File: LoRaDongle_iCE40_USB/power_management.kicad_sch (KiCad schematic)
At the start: 17 parts, among them U1 RP550K0001A-TR

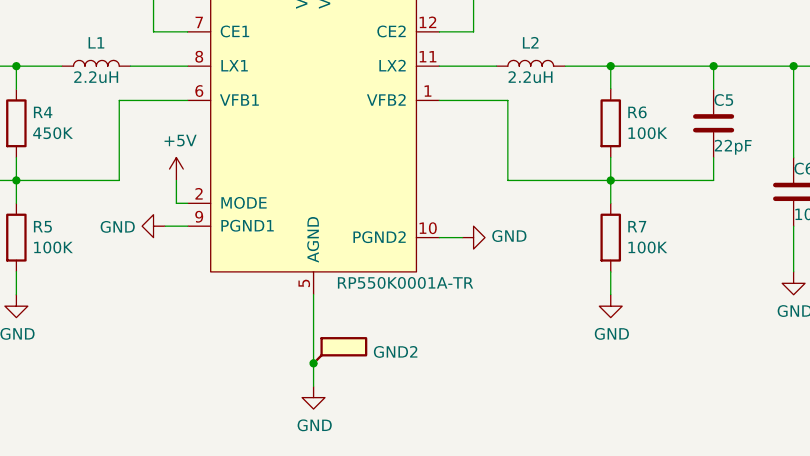
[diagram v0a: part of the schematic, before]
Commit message: updating symbol details
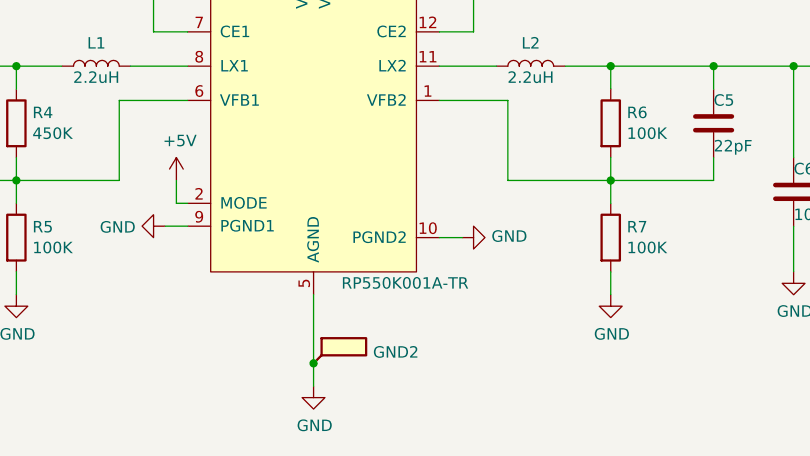
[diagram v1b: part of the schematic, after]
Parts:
- 1V2, 3V3, GND2: Manufacturer (none) -> -; Manufacturer Part Number (none) -> -; Package (none) -> -; Type (none) -> -
- C2, C4, C6: Manufacturer Part Number (none) -> Out of Stock find New; Package (none) -> 0603; Type (none) -> SMD
- C3, C5: Manufacturer (none) -> Murata Electronics; Manufacturer Part Number (none) -> GRM1555C1H220FA01D; Package (none) -> 0402; Type (none) -> SMD
- L1, L2: Manufacturer (none) -> Taiyo Yuden; Manufacturer Part Number (none) -> MCHK1608T2R2MKN; Package (none) -> 0603; Physical Size 1008 -> (none); Type (none) -> SMD
- U1: value RP550K0001A-TR -> RP550K001A-TR; Manufacturer (none) -> Nisshinbo Micro Devices Inc.; Manufacturer Part Number (none) -> RP550K001A-TR; Package (none) -> DFN(PLP)2730-12; Type (none) -> SMD
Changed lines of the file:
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@@
     (in_bom yes) (on_board yes)
     (property "Reference" "U1" (id 0) (at 139.7 77.47 0))
-    (property "Value" "RP550K0001A-TR" (id 1) (at 161.29 113.03 0))
+    (property "Value" "RP550K001A-TR" (id 1) (at 161.29 113.03 0))
     (property "Footprint" "RP550K001A-TR_KiCad:SON50P270X300X60-13N" (id 2) (at 137.16 80.01 0)
       (effects (font (size 1.27 1.27)) hide)
     )
     (property "Datasheet" "" (id 3) (at 137.16 80.01 0)
+      (effects (font (size 1.27 1.27)) hide)
+    )
+    (property "Description" "BUCK DC/DC CONVERTER DUAL OUTPUT" (id 4) (at 151.13 96.52 0)
+      (effects (font (size 1.27 1.27)) hide)
+    )
+    (property "Manufacturer" "Nisshinbo Micro Devices Inc." (id 5) (at 151.13 96.52 0)
+      (effects (font (size 1.27 1.27)) hide)
+    )
+    (property "Manufacturer Part Number" "RP550K001A-TR" (id 6) (at 151.13 96.52 0)
+      (effects (font (size 1.27 1.27)) hide)
+    )
+    (property "Package" "DFN(PLP)2730-12" (id 7) (at 151.13 96.52 0)
+      (effects (font (size 1.27 1.27)) hide)
+    )
+    (property "Type" "SMD" (id 8) (at 151.13 96.52 0)
       (effects (font (size 1.27 1.27)) hide)
     )
@@
       (effects (font (size 1.27 1.27)) hide)
     )
+    (property "Description" "CAP CER 22PF 50V C0G/NP0 0402" (id 5) (at 106.68 95.25 0)
+      (effects (font (size 1.27 1.27)) hide)
+    )
+    (property "Manufacturer" "Murata Electronics" (id 6) (at 106.68 95.25 0)
+      (effects (font (size 1.27 1.27)) hide)
+    )
+    (property "Manufacturer Part Number" "GRM1555C1H220FA01D" (id 7) (at 106.68 95.25 0)
+      (effects (font (size 1.27 1.27)) hide)
+    )
+    (property "Package" "0402" (id 8) (at 106.68 95.25 0)
+      (effects (font (size 1.27 1.27)) hide)
+    )
+    (property "Type" "SMD" (id 9) (at 106.68 95.25 0)
+      (effects (font (size 1.27 1.27)) hide)
+    )
     (pin "1")
     (pin "2")
@@
     )
     (property "Physical size" "0603" (id 5) (at 97.79 102.87 0)
+      (effects (font (size 1.27 1.27)) hide)
+    )
+    (property "Manufacturer Part Number" "Out of Stock find New" (id 6) (at 97.79 102.87 0)
+      (effects (font (size 1.27 1.27)) hide)
+    )
+    (property "Package" "0603" (id 7) (at 97.79 102.87 0)
+      (effects (font (size 1.27 1.27)) hide)
+    )
+    (property "Type" "SMD" (id 8) (at 97.79 102.87 0)
       (effects (font (size 1.27 1.27)) hide)
     )
@@
       (effects (font (size 1.27 1.27)) hide)
     )
+    (property "Description" "Test Point" (id 4) (at 93.98 88.9 0)
+      (effects (font (size 1.27 1.27)) hide)
+    )
+    (property "Manufacturer" "-" (id 5) (at 93.98 88.9 0)
+      (effects (font (size 1.27 1.27)) hide)
+    )
+    (property "Manufacturer Part Number" "-" (id 6) (at 93.98 88.9 0)
+      (effects (font (size 1.27 1.27)) hide)
+    )
+    (property "Package" "-" (id 7) (at 93.98 88.9 0)
+      (effects (font (size 1.27 1.27)) hide)
+    )
+    (property "Type" "-" (id 8) (at 93.98 88.9 0)
+      (effects (font (size 1.27 1.27)) hide)
+    )
     (pin "1")
   )
@@
       (effects (font (size 1.27 1.27)) hide)
     )
+    (property "Description" "Test Point" (id 4) (at 209.55 88.9 0)
+      (effects (font (size 1.27 1.27)) hide)
+    )
+    (property "Manufacturer" "-" (id 5) (at 209.55 88.9 0)
+      (effects (font (size 1.27 1.27)) hide)
+    )
+    (property "Manufacturer Part Number" "-" (id 6) (at 209.55 88.9 0)
+      (effects (font (size 1.27 1.27)) hide)
+    )
+    (property "Package" "-" (id 7) (at 209.55 88.9 0)
+      (effects (font (size 1.27 1.27)) hide)
+    )
+    (property "Type" "-" (id 8) (at 209.55 88.9 0)
+      (effects (font (size 1.27 1.27)) hide)
+    )
     (pin "1")
   )
@@
       (effects (font (size 1.27 1.27)) hide)
     )
+    (property "Description" "Test Point" (id 4) (at 151.13 121.92 0)
+      (effects (font (size 1.27 1.27)) hide)
+    )
+    (property "Manufacturer" "-" (id 5) (at 151.13 121.92 0)
+      (effects (font (size 1.27 1.27)) hide)
+    )
+    (property "Manufacturer Part Number" "-" (id 6) (at 151.13 121.92 0)
+      (effects (font (size 1.27 1.27)) hide)
+    )
+    (property "Package" "-" (id 7) (at 151.13 121.92 0)
+      (effects (font (size 1.27 1.27)) hide)
+    )
+    (property "Type" "-" (id 8) (at 151.13 121.92 0)
+      (effects (font (size 1.27 1.27)) hide)
+    )
     (pin "1")
   )
@@
       (effects (font (size 1.27 1.27)) hide)
     )
+    (property "Manufacturer Part Number" "Out of Stock find New" (id 6) (at 204.47 102.87 0)
+      (effects (font (size 1.27 1.27)) hide)
+    )
+    (property "Package" "0603" (id 7) (at 204.47 102.87 0)
+      (effects (font (size 1.27 1.27)) hide)
+    )
+    (property "Type" "SMD" (id 8) (at 204.47 102.87 0)
+      (effects (font (size 1.27 1.27)) hide)
+    )
     (pin "1")
     (pin "2")
@@
       (effects (font (size 1.27 1.27)) hide)
     )
+    (property "Description" "CAP CER 22PF 50V C0G/NP0 0402" (id 5) (at 195.58 95.25 0)
+      (effects (font (size 1.27 1.27)) hide)
+    )
+    (property "Manufacturer" "Murata Electronics" (id 6) (at 195.58 95.25 0)
+      (effects (font (size 1.27 1.27)) hide)
+    )
+    (property "Manufacturer Part Number" "GRM1555C1H220FA01D" (id 7) (at 195.58 95.25 0)
+      (effects (font (size 1.27 1.27)) hide)
+    )
+    (property "Package" "0402" (id 8) (at 195.58 95.25 0)
+      (effects (font (size 1.27 1.27)) hide)
+    )
+    (property "Type" "SMD" (id 9) (at 195.58 95.25 0)
+      (effects (font (size 1.27 1.27)) hide)
+    )
     (pin "1")
     (pin "2")
@@
     )
     (property "Physical size" "0603" (id 5) (at 115.57 69.85 0)
+      (effects (font (size 1.27 1.27)) hide)
+    )
+    (property "Manufacturer Part Number" "Out of Stock find New" (id 6) (at 115.57 69.85 0)
+      (effects (font (size 1.27 1.27)) hide)
+    )
+    (property "Package" "0603" (id 7) (at 115.57 69.85 0)
+      (effects (font (size 1.27 1.27)) hide)
+    )
+    (property "Type" "SMD" (id 8) (at 115.57 69.85 0)
       (effects (font (size 1.27 1.27)) hide)
     )
@@
       (effects (font (size 1.27 1.27)) hide)
     )
-    (property "Physical Size" "1008" (id 5) (at 175.26 88.9 90)
+    (property "Physical Size" "" (id 5) (at 175.26 88.9 90)
+      (effects (font (size 1.27 1.27)) hide)
+    )
+    (property "Description" "FIXED IND 2.2UH 1.2A 292MOHM SMD" (id 6) (at 175.26 88.9 0)
+      (effects (font (size 1.27 1.27)) hide)
+    )
+    (property "Manufacturer" "Taiyo Yuden" (id 7) (at 175.26 88.9 0)
+      (effects (font (size 1.27 1.27)) hide)
+    )
+    (property "Manufacturer Part Number" "MCHK1608T2R2MKN" (id 8) (at 175.26 88.9 0)
+      (effects (font (size 1.27 1.27)) hide)
+    )
+    (property "Package" "0603" (id 9) (at 175.26 88.9 0)
+      (effects (font (size 1.27 1.27)) hide)
+    )
+    (property "Type" "SMD" (id 10) (at 175.26 88.9 0)
       (effects (font (size 1.27 1.27)) hide)
     )
@@
       (effects (font (size 1.27 1.27)) hide)
     )
-    (property "Physical Size" "1008" (id 5) (at 127 88.9 90)
-      (effects (font (size 1.27 1.27)) hide)
-    )
+    (property "Physical Size" "" (id 5) (at 127 88.9 90)
+      (effects (font (size 1.27 1.27)) hide)
+    )
+    (property "Description" "FIXED IND 2.2UH 1.2A 292MOHM SMD" (id 6) (at 127 88.9 0)
+      (effects (font (size 1.27 1.27)) hide)
+    )
+    (property "Manufacturer" "Taiyo Yuden" (id 7) (at 127 88.9 0)
+      (effects (font (size 1.27 1.27)) hide)
+    )
+    (property "Manufacturer Part Number" "MCHK1608T2R2MKN" (id 8) (at 127 88.9 0)
+      (effects (font (size 1.27 1.27)) hide)
+    )
+    (property "Package" "0603" (id 9) (at 127 88.9 0)
+      (effects (font (size 1.27 1.27)) hide)
+    )
+    (property "Type" "SMD" (id 10) (at 127 88.9 0)
+      (effects (font (size 1.27 1.27)) hide)
+    )

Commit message: updated BOM
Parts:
- C2, C4, C6: Manufacturer (none) -> Murata Electronics; Manufacturer Part Number Out of Stock find New -> GRM188R60J106ME47D
- D1: value LED -> PWR; footprint LED_SMD:LED_0603_1608Metric_Pad1.05x0.95mm_HandSolder -> LED_SMD:LED_0805_2012Metric_Pad1.15x1.40mm_HandSolder; Manufacturer (none) -> SunLED; Manufacturer Part Number (none) -> XZM2CRK54WA-8; Package (none) -> 0805
- R3: value R -> 100R; Manufacturer (none) -> Stackpole Electronics Inc; Manufacturer Part Number (none) -> RMCF0402FT100R; Package (none) -> 0402
- R4: value 450K -> 453K; Manufacturer (none) -> Stackpole Electronics Inc; Manufacturer Part Number (none) -> RMCF0402FT453K
- R5, R6, R7: Manufacturer (none) -> Stackpole Electronics Inc; Manufacturer Part Number (none) -> RMCF0402JT100K
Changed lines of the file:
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@@
+      (effects (font (size 1.27 1.27)) hide)
+    )
+    (property "Description" "RES 100K OHM 5% 1/16W 0402" (id 4) (at 184.15 95.25 0)
+      (effects (font (size 1.27 1.27)) hide)
+    )
+    (property "Manufacturer" "Stackpole Electronics Inc" (id 5) (at 184.15 95.25 0)
+      (effects (font (size 1.27 1.27)) hide)
+    )
+    (property "Manufacturer Part Number" "RMCF0402JT100K" (id 6) (at 184.15 95.25 0)
       (effects (font (size 1.27 1.27)) hide)
     )
@@
     )
     (property "Datasheet" "~" (id 3) (at 184.15 107.95 0)
+      (effects (font (size 1.27 1.27)) hide)
+    )
+    (property "Description" "RES 100K OHM 5% 1/16W 0402" (id 4) (at 184.15 107.95 0)
+      (effects (font (size 1.27 1.27)) hide)
+    )
+    (property "Manufacturer" "Stackpole Electronics Inc" (id 5) (at 184.15 107.95 0)
+      (effects (font (size 1.27 1.27)) hide)
+    )
+    (property "Manufacturer Part Number" "RMCF0402JT100K" (id 6) (at 184.15 107.95 0)
       (effects (font (size 1.27 1.27)) hide)
     )
@@
       (effects (font (size 1.27 1.27)) (justify left))
     )
-    (property "Value" "450K" (id 1) (at 119.888 96.393 0)
+    (property "Value" "453K" (id 1) (at 119.888 96.393 0)
       (effects (font (size 1.27 1.27)) (justify left))
     )
@@
       (effects (font (size 1.27 1.27)) hide)
     )
+    (property "Description" "RES 453K OHM 1% 1/16W 0402" (id 4) (at 118.11 95.25 0)
+      (effects (font (size 1.27 1.27)) hide)
+    )
+    (property "Manufacturer" "Stackpole Electronics Inc" (id 5) (at 118.11 95.25 0)
+      (effects (font (size 1.27 1.27)) hide)
+    )
+    (property "Manufacturer Part Number" "RMCF0402FT453K" (id 6) (at 118.11 95.25 0)
+      (effects (font (size 1.27 1.27)) hide)
+    )
     (pin "1")
     (pin "2")
@@
       (effects (font (size 1.27 1.27)) hide)
     )
+    (property "Description" "RES 100K OHM 5% 1/16W 0402" (id 4) (at 118.11 107.95 0)
+      (effects (font (size 1.27 1.27)) hide)
+    )
+    (property "Manufacturer" "Stackpole Electronics Inc" (id 5) (at 118.11 107.95 0)
+      (effects (font (size 1.27 1.27)) hide)
+    )
+    (property "Manufacturer Part Number" "RMCF0402JT100K" (id 6) (at 118.11 107.95 0)
+      (effects (font (size 1.27 1.27)) hide)
+    )
     (pin "1")
     (pin "2")
@@
       (effects (font (size 1.27 1.27)) hide)
     )
-    (property "Manufacturer Part Number" "Out of Stock find New" (id 6) (at 97.79 102.87 0)
+    (property "Manufacturer Part Number" "GRM188R60J106ME47D" (id 6) (at 97.79 102.87 0)
       (effects (font (size 1.27 1.27)) hide)
     )
@@
     )
     (property "Type" "SMD" (id 8) (at 97.79 102.87 0)
+      (effects (font (size 1.27 1.27)) hide)
+    )
+    (property "Description" "CAP CER 10UF 6.3V X5R 0603" (id 9) (at 97.79 102.87 0)
+      (effects (font (size 1.27 1.27)) hide)
+    )
+    (property "Manufacturer" "Murata Electronics" (id 10) (at 97.79 102.87 0)
       (effects (font (size 1.27 1.27)) hide)
     )
@@
       (effects (font (size 1.27 1.27)) (justify left))
     )
-    (property "Value" "R" (id 1) (at 56.388 96.393 0)
+    (property "Value" "100R" (id 1) (at 56.388 96.393 0)
       (effects (font (size 1.27 1.27)) (justify left))
     )
@@
       (effects (font (size 1.27 1.27)) hide)
     )
+    (property "Description" "RES 100 OHM 1% 1/16W 0402" (id 4) (at 54.61 95.25 0)
+      (effects (font (size 1.27 1.27)) hide)
+    )
+    (property "Manufacturer" "Stackpole Electronics Inc" (id 5) (at 54.61 95.25 0)
+      (effects (font (size 1.27 1.27)) hide)
+    )
+    (property "Manufacturer Part Number" "RMCF0402FT100R" (id 6) (at 54.61 95.25 0)
+      (effects (font (size 1.27 1.27)) hide)
+    )
+    (property "Package" "0402" (id 7) (at 54.61 95.25 0)
+      (effects (font (size 1.27 1.27)) hide)
+    )
     (pin "1")
     (pin "2")
@@
       (effects (font (size 1.27 1.27)) (justify right))
     )
-    (property "Value" "LED" (id 1) (at 57.6072 105.4608 90)
-      (effects (font (size 1.27 1.27)) (justify right))
-    )
-    (property "Footprint" "LED_SMD:LED_0603_1608Metric_Pad1.05x0.95mm_HandSolder" (id 2) (at 54.61 104.14 0)
+    (property "Value" "PWR" (id 1) (at 57.6072 105.4608 90)
+      (effects (font (size 1.27 1.27)) (justify right))
+    )
+    (property "Footprint" "LED_SMD:LED_0805_2012Metric_Pad1.15x1.40mm_HandSolder" (id 2) (at 54.61 104.14 0)
       (effects (font (size 1.27 1.27)) hide)
     )
     (property "Datasheet" "~" (id 3) (at 54.61 104.14 0)
+      (effects (font (size 1.27 1.27)) hide)
+    )
+    (property "Description" "LED RED CLEAR CHIP SMD" (id 4) (at 54.61 104.14 0)
+      (effects (font (size 1.27 1.27)) hide)
+    )
+    (property "Manufacturer" "SunLED" (id 5) (at 54.61 104.14 0)
+      (effects (font (size 1.27 1.27)) hide)
+    )
+    (property "Manufacturer Part Number" "XZM2CRK54WA-8" (id 6) (at 54.61 104.14 0)
+      (effects (font (size 1.27 1.27)) hide)
+    )
+    (property "Package" "0805" (id 7) (at 54.61 104.14 0)
       (effects (font (size 1.27 1.27)) hide)
     )
@@
       (effects (font (size 1.27 1.27)) hide)
     )
-    (property "Manufacturer Part Number" "Out of Stock find New" (id 6) (at 204.47 102.87 0)
+    (property "Manufacturer Part Number" "GRM188R60J106ME47D" (id 6) (at 204.47 102.87 0)
       (effects (font (size 1.27 1.27)) hide)
     )
@@
       (effects (font (size 1.27 1.27)) hide)
     )
+    (property "Description" "CAP CER 10UF 6.3V X5R 0603" (id 9) (at 204.47 102.87 0)
+      (effects (font (size 1.27 1.27)) hide)
+    )
+    (property "Manufacturer" "Murata Electronics" (id 10) (at 204.47 102.87 0)
+      (effects (font (size 1.27 1.27)) hide)
+    )
     (pin "1")
     (pin "2")
@@
       (effects (font (size 1.27 1.27)) hide)
     )
-    (property "Manufacturer Part Number" "Out of Stock find New" (id 6) (at 115.57 69.85 0)
+    (property "Manufacturer Part Number" "GRM188R60J106ME47D" (id 6) (at 115.57 69.85 0)
       (effects (font (size 1.27 1.27)) hide)
     )
@@
       (effects (font (size 1.27 1.27)) hide)
     )
+    (property "Description" "CAP CER 10UF 6.3V X5R 0603" (id 9) (at 115.57 69.85 0)
+      (effects (font (size 1.27 1.27)) hide)
+    )
+    (property "Manufacturer" "Murata Electronics" (id 10) (at 115.57 69.85 0)
+      (effects (font (size 1.27 1.27)) hide)
+    )

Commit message: generate raw bom csv from kicad
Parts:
- R4, R5, R6, R7: Package (none) -> 0402
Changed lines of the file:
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@@
+      (effects (font (size 1.27 1.27)) hide)
+    )
+    (property "Package" "0402" (id 7) (at 184.15 95.25 0)
       (effects (font (size 1.27 1.27)) hide)
     )
@@
     )
     (property "Manufacturer Part Number" "RMCF0402JT100K" (id 6) (at 184.15 107.95 0)
+      (effects (font (size 1.27 1.27)) hide)
+    )
+    (property "Package" "0402" (id 7) (at 184.15 107.95 0)
       (effects (font (size 1.27 1.27)) hide)
     )
@@
       (effects (font (size 1.27 1.27)) hide)
     )
+    (property "Package" "0402" (id 7) (at 118.11 95.25 0)
+      (effects (font (size 1.27 1.27)) hide)
+    )
     (pin "1")
     (pin "2")
@@
       (effects (font (size 1.27 1.27)) hide)
     )
+    (property "Package" "0402" (id 7) (at 118.11 107.95 0)
+      (effects (font (size 1.27 1.27)) hide)
+    )

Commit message: updating silkscreen
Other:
- title: LoRa Dongle -> RiscVLoRaDongle
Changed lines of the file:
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@@
   (paper "A4")
   (title_block
-    (title "LoRa Dongle")
+    (title "RiscVLoRaDongle")
+    (date "2022-02-03")
+    (rev "1.0")
     (company "Mark Njoroge")
   )
@@
   )
   (junction (at 184.15 88.9) (diameter 0) (color 0 0 0 0)
+  )
+  (junction (at 115.57 63.5) (diameter 0) (color 0 0 0 0)
   )
   (junction (at 195.58 88.9) (diameter 0) (color 0 0 0 0)
@@
     (pin "2")
   )
+  (symbol (lib_id "power:PWR_FLAG") (at 115.57 63.5 270) (unit 1)
+    (in_bom yes) (on_board yes) (fields_autoplaced)
+    (property "Reference" "#FLG03" (id 0) (at 117.475 63.5 0)
+      (effects (font (size 1.27 1.27)) hide)
+    )
+    (property "Value" "PWR_FLAG" (id 1) (at 119.38 63.4999 90)
+      (effects (font (size 1.27 1.27)) (justify left))
+    )
+    (property "Footprint" "" (id 2) (at 115.57 63.5 0)
+      (effects (font (size 1.27 1.27)) hide)
+    )
+    (property "Datasheet" "~" (id 3) (at 115.57 63.5 0)
+      (effects (font (size 1.27 1.27)) hide)
+    )
+    (pin "1")
+  )
 )
